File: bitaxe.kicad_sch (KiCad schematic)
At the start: 92 parts, among them IC1 BM1387, IC2 BM1387, IC3 MIC5317, IC4 MIC5317, J1 USB_OTG, J2 Conn_01x02, J3 Conn_01x05, J4 Conn_01x02, J5 Conn_01x03, U1 DT1452-02SO-7, U2 FT231XQ, Y1 25MHz

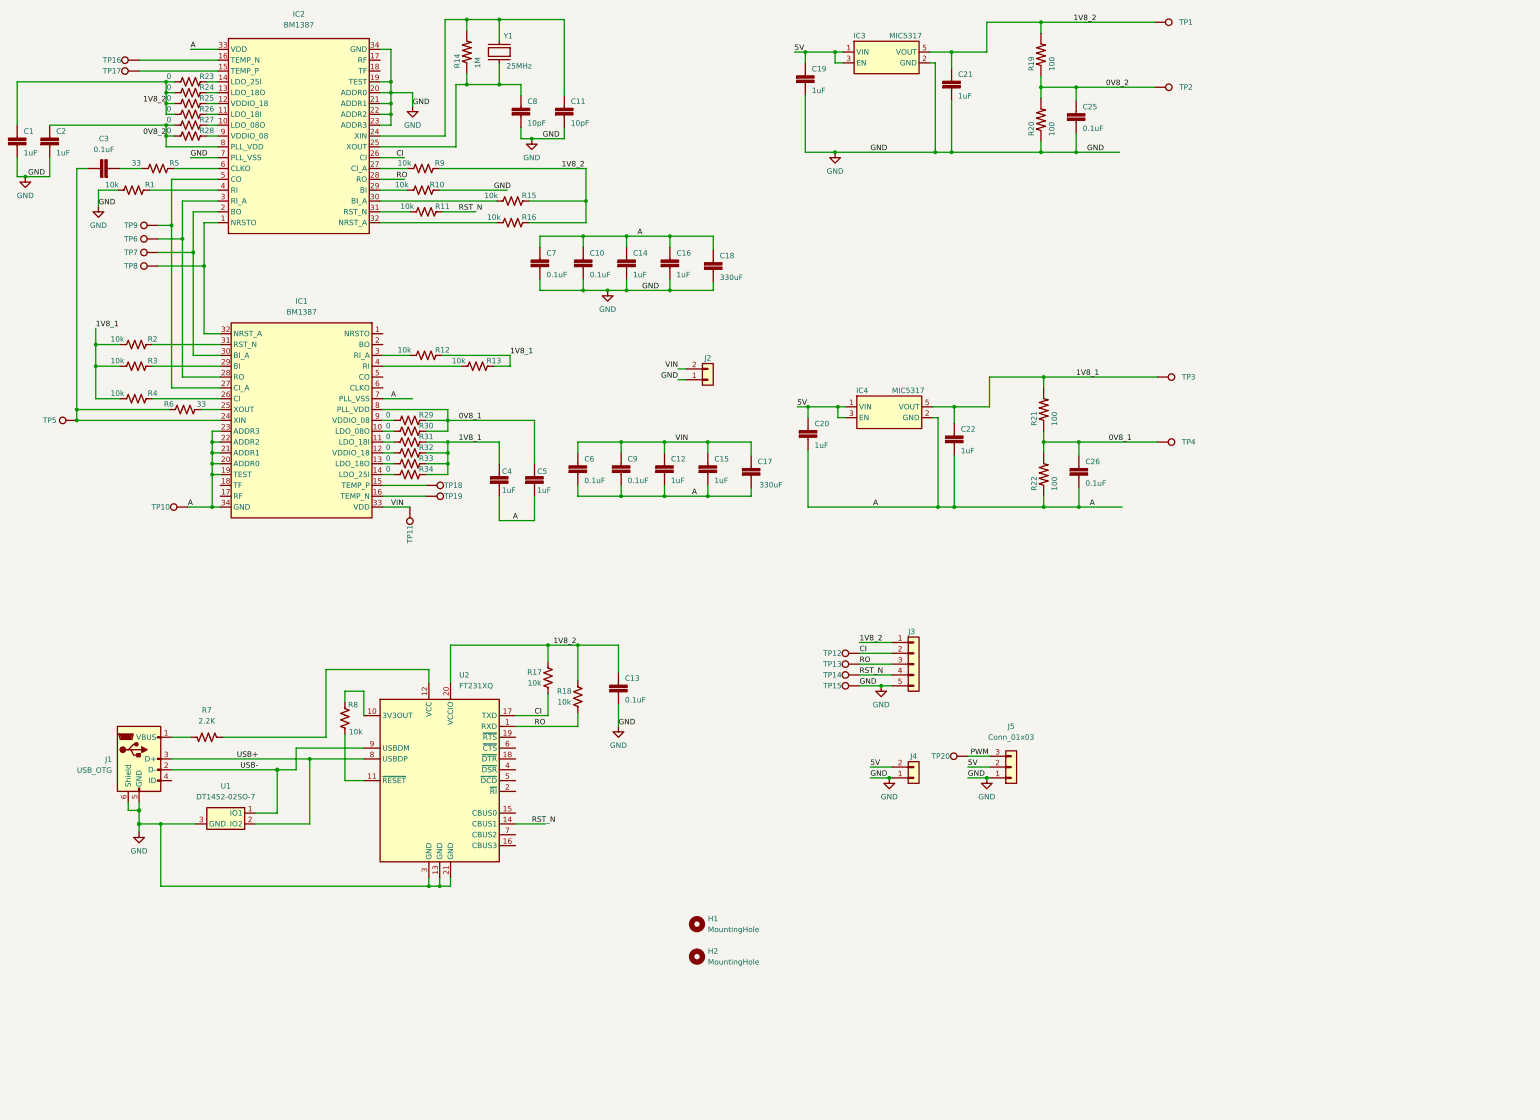
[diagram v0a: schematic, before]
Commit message: routed the bitaxe!
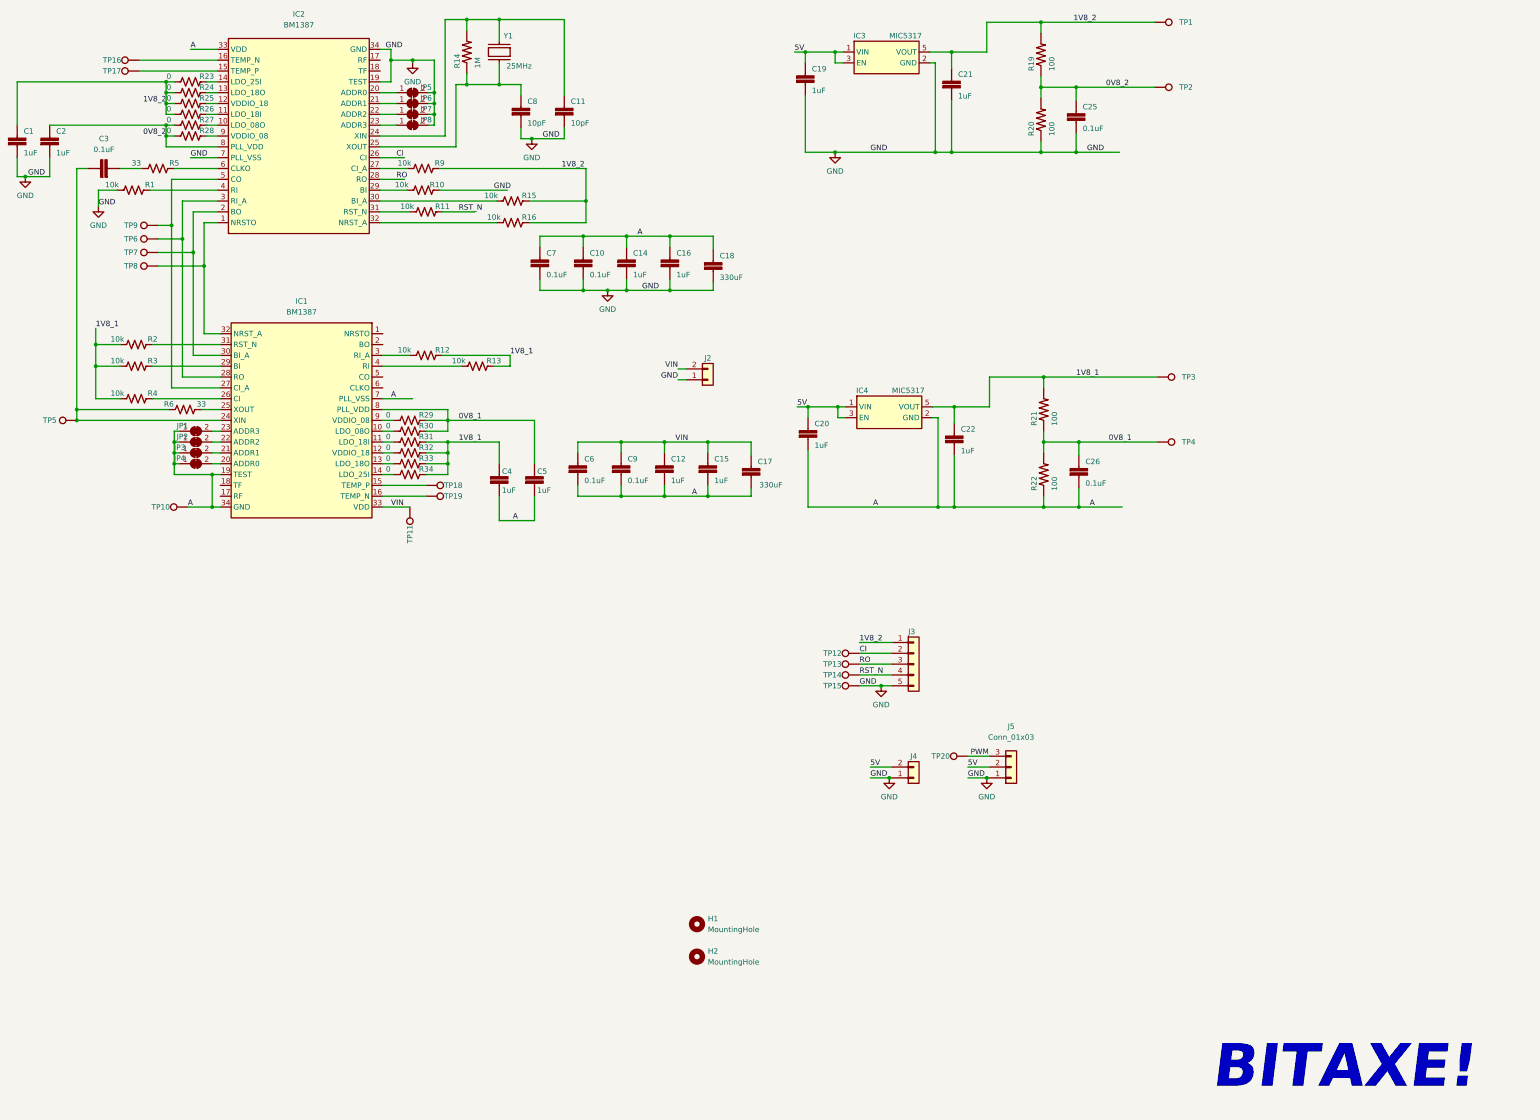
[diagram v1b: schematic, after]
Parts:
- removed C13: 311-3342-1-ND, DayMiner:C0402, symbol DayMiner-eagle-import:CAP0402
- removed J1: USB_OTG, DayMiner:USB_Micro-B_EDAC_UCON00686, symbol Connector:USB_OTG
- removed R17, R18, R8: 10k, DayMiner:R0402, symbol Device:R_US
- removed R7: 2.2K, DayMiner:R0402, symbol Device:R_US
- removed U1: DT1452-02SO-7, Package_TO_SOT_SMD:SOT-23, symbol CM4IO:DT1452-02SO-7
- removed U2: FT231XQ, Package_DFN_QFN:QFN-20-1EP_4x4mm_P0.5mm_EP2.5x2.5mm, symbol Interface_USB:FT231XQ
- added JP1, JP2, JP3, JP4, JP5, JP6, JP7, JP8: SolderJumper_2_Bridged, Jumper:SolderJumper-2_P1.3mm_Bridged2Bar_RoundedPad1.0x1.5mm, symbol Jumper:SolderJumper_2_Bridged
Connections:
- net A: now also JP1.1 (A), JP2.1 (A), JP3.1 (A), JP4.1 (A); no longer IC1.20 (ADDR0), IC1.21 (ADDR1), IC1.22 (ADDR2), IC1.23 (ADDR3)
- net GND: now also JP5.2 (B), JP6.2 (B), JP7.2 (B), JP8.2 (B); no longer IC2.20 (ADDR0), IC2.21 (ADDR1), IC2.22 (ADDR2), IC2.23 (ADDR3)
- new net: IC2.22 (ADDR2), JP7.1 (A)
- new net: IC2.21 (ADDR1), JP6.1 (A)
- new net: IC2.23 (ADDR3), JP8.1 (A)
- new net: IC2.20 (ADDR0), JP5.1 (A)
- new net: IC1.21 (ADDR1), JP3.2 (B)
- new net: IC1.22 (ADDR2), JP2.2 (B)
- new net: IC1.20 (ADDR0), JP4.2 (B)
- new net: IC1.23 (ADDR3), JP1.2 (B)
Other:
- note added: "BITAXE!"

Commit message: updated BOM and manufacturing files
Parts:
- C17, C18: DK 2388-PCT330/10DM-ND -> TCJD337M010R0025
- C3: DK (none) -> 1292-1639-1-ND
- H1, H2, JP1, JP2, JP3, JP4, JP5, JP6, JP7, JP8: DNP (none) -> T
- R1, R10, R11, R12, R13, R15, R16, R2, R3, R4, R9: DK (none) -> RMCF0402FT10K0CT-ND
- R22: DK RMCF0402FT10K0CT-ND -> RMCF0402FT12K4CT-ND
- R23, R24, R25, R26, R27, R28, R29, R30, R31, R32, R33, R34: DK (none) -> RMCF0402ZT0R00CT-ND
- R5, R6: DK (none) -> 311-33.0LRCT-ND
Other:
- moved on the sheet: C1, C10, C11, C12, C14, C15, C16, C17, C18, C19, C2, C20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
